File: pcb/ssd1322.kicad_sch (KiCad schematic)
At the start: 11 parts, among them J10 SSD1322 30-Pin Connector, J8 Display Connector Input, J9 Display Connector Output

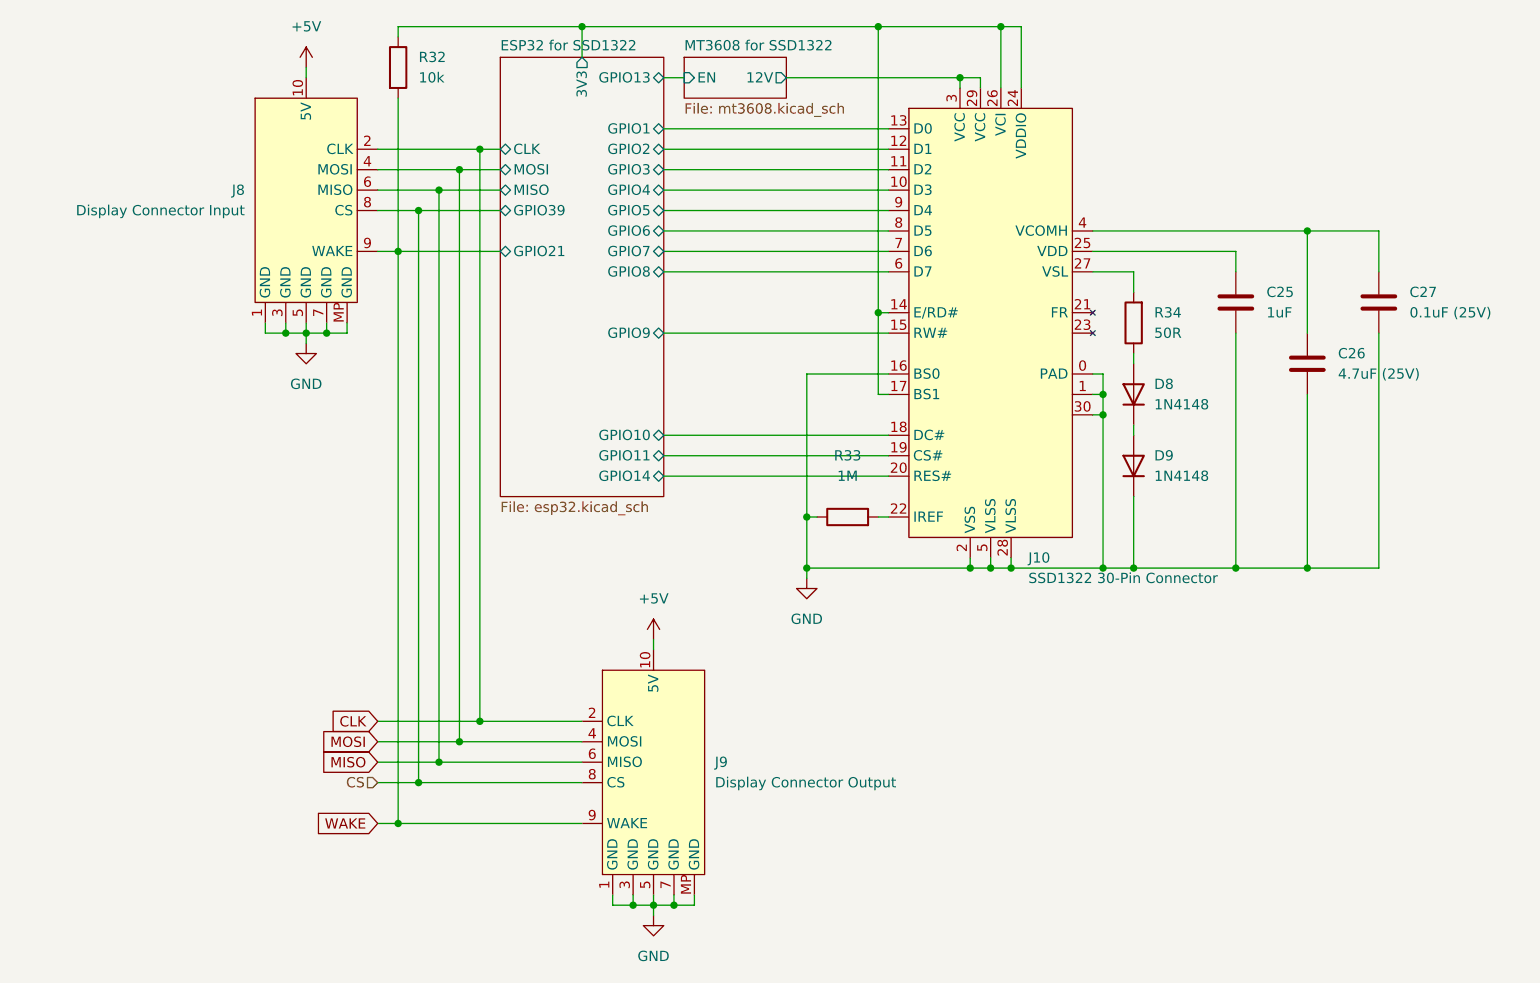
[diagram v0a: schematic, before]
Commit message: Split PCB into modules
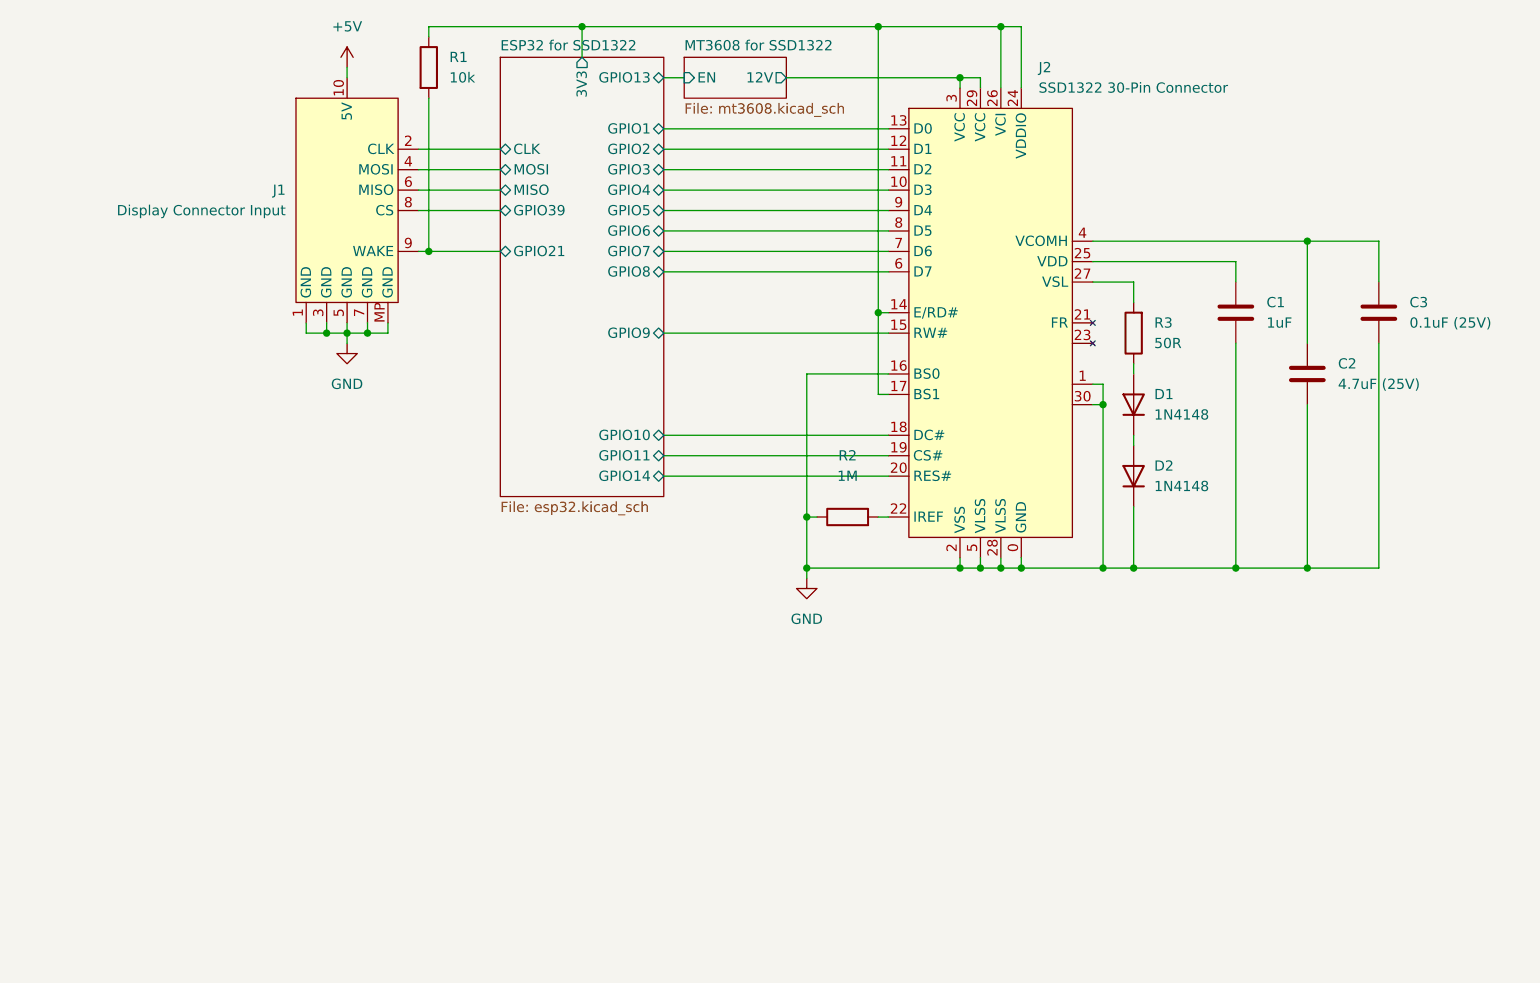
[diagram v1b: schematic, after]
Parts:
- removed J9: Display Connector Output, Connector_Molex:Molex_PicoBlade_53261-1071_1x10-1MP_P1.25mm_Horizontal, symbol Data Connector:Display_Connector_Output
- J2: renamed from J10; footprint Connector_FFC-FPC:TE_3-1734839-0_1x30-1MP_P0.5mm_Horizontal -> Display_FPC:ssd1322
- renumbered C25 to C1, C26 to C2, C27 to C3, D8 to D1, D9 to D2, J8 to J1, R32 to R1, R33 to R2, R34 to R3
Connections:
- net CLK renamed ESP32 for SSD1322/CLK
- net CS renamed ESP32 for SSD1322/GPIO39
- net MISO renamed ESP32 for SSD1322/MISO
- net MOSI renamed ESP32 for SSD1322/MOSI
- net WAKE renamed ESP32 for SSD1322/GPIO21
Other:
- moved on the sheet: C1, C2, C3, D1, D2, J1, R1, R3

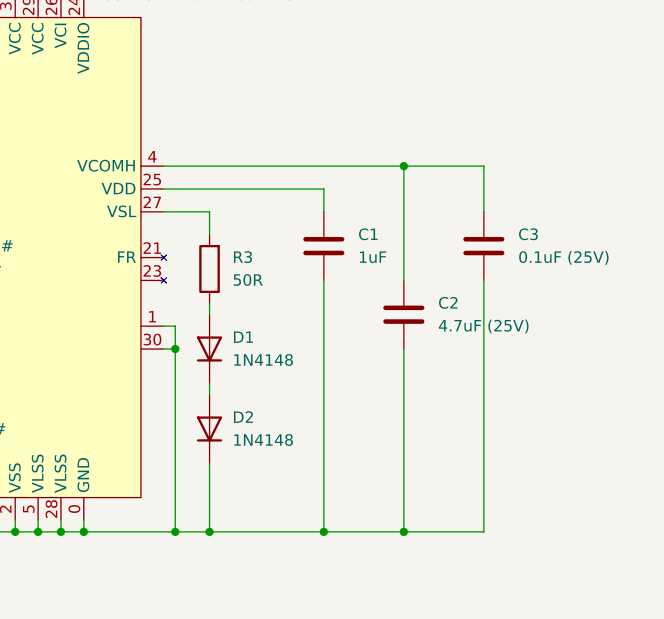
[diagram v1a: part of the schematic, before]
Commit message: Master board PCB routing
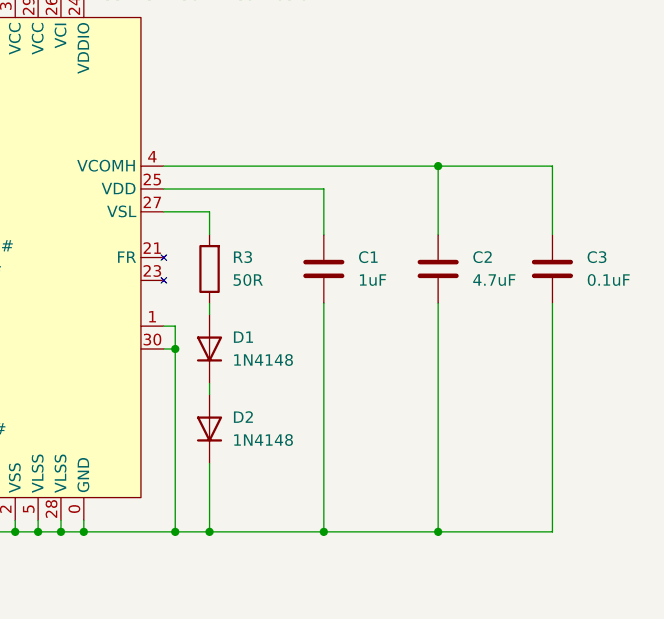
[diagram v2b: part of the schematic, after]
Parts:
- C2: value 4.7uF (25V) -> 4.7uF
- C3: value 0.1uF (25V) -> 0.1uF
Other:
- moved on the sheet: C1, C2, C3
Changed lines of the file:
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@@
+	)
+	(junction
+		(at 180.34 60.96)
+		(diameter 0)
+		(color 0 0 0 0)
+	)
+	(junction
+		(at 180.34 101.6)
+		(diameter 0)
+		(color 0 0 0 0)
 	)
 	(junction
@@
 	)
 	(junction
-		(at 176.53 101.6)
-		(diameter 0)
-		(color 0 0 0 0)
-	)
-	(junction
 		(at 123.19 69.85)
 		(diameter 0)
@@
 	)
 	(junction
-		(at 176.53 60.96)
-		(diameter 0)
-		(color 0 0 0 0)
-	)
-	(junction
 		(at 133.35 101.6)
 		(diameter 0)
@@
 	(wire
 		(pts
+			(xy 180.34 60.96) (xy 193.04 60.96)
+		)
+		(stroke
+			(width 0)
+			(type default)
+		)
+	)
+	(wire
+		(pts
 			(xy 149.86 66.04) (xy 154.94 66.04)
 		)
@@
 	(wire
 		(pts
-			(xy 176.53 60.96) (xy 176.53 73.66)
+			(xy 180.34 60.96) (xy 180.34 68.58)
 		)
 		(stroke
@@
 	(wire
 		(pts
-			(xy 176.53 81.28) (xy 176.53 101.6)
+			(xy 180.34 76.2) (xy 180.34 101.6)
 		)
 		(stroke
@@
 	(wire
 		(pts
-			(xy 176.53 60.96) (xy 185.42 60.96)
-		)
-		(stroke
-			(width 0)
-			(type default)
-		)
-	)
-	(wire
-		(pts
 			(xy 123.19 95.25) (xy 124.46 95.25)
 		)
@@
 	(wire
 		(pts
+			(xy 180.34 101.6) (xy 193.04 101.6)
+		)
+		(stroke
+			(width 0)
+			(type default)
+		)
+	)
+	(wire
+		(pts
 			(xy 135.89 101.6) (xy 138.43 101.6)
 		)
@@
 	(wire
 		(pts
-			(xy 167.64 63.5) (xy 167.64 66.04)
+			(xy 167.64 63.5) (xy 167.64 68.58)
 		)
 		(stroke
@@
 	(wire
 		(pts
-			(xy 167.64 101.6) (xy 176.53 101.6)
+			(xy 167.64 101.6) (xy 180.34 101.6)
 		)
 		(stroke
@@
 	(wire
 		(pts
-			(xy 176.53 101.6) (xy 185.42 101.6)
-		)
-		(stroke
-			(width 0)
-			(type default)
-		)
-	)
-	(wire
-		(pts
 			(xy 66.04 49.53) (xy 76.2 49.53)
 		)
@@
 	(wire
 		(pts
-			(xy 167.64 73.66) (xy 167.64 101.6)
+			(xy 167.64 76.2) (xy 167.64 101.6)
 		)
 		(stroke
@@
 	(wire
 		(pts
-			(xy 149.86 60.96) (xy 176.53 60.96)
+			(xy 149.86 60.96) (xy 180.34 60.96)
 		)
 		(stroke
@@
 	(wire
 		(pts
-			(xy 185.42 73.66) (xy 185.42 101.6)
+			(xy 193.04 76.2) (xy 193.04 101.6)
 		)
 		(stroke
@@
 	(wire
 		(pts
-			(xy 185.42 60.96) (xy 185.42 66.04)
+			(xy 193.04 60.96) (xy 193.04 68.58)
 		)
 		(stroke
@@
 	(symbol
 		(lib_id "Device:C")
-		(at 167.64 69.85 0)
+		(at 167.64 72.39 0)
 		(unit 1)
 		(exclude_from_sim no)
@@
 		(fields_autoplaced yes)
 		(property "Reference" "C1"
-			(at 171.45 68.5799 0)
+			(at 171.45 71.1199 0)
 			(effects
 				(font
@@
 		)
 		(property "Value" "1uF"
-			(at 171.45 71.1199 0)
+			(at 171.45 73.6599 0)
 			(effects
 				(font
@@
 		)
 		(property "Footprint" "Capacitor_SMD:C_0603_1608Metric"
-			(at 168.6052 73.66 0)
+			(at 168.6052 76.2 0)
 			(effects
 				(font
@@
 		)
 		(property "Datasheet" "~"
-			(at 167.64 69.85 0)
+			(at 167.64 72.39 0)
 			(effects
 				(font
@@
 		)
 		(property "Description" "Unpolarized capacitor"
-			(at 167.64 69.85 0)
+			(at 167.64 72.39 0)
 			(effects
 				(font
@@
 	(symbol
 		(lib_id "Device:C")
-		(at 185.42 69.85 0)
+		(at 193.04 72.39 0)
 		(unit 1)
 		(exclude_from_sim no)
@@
 		(fields_autoplaced yes)
 		(property "Reference" "C3"
-			(at 189.23 68.5799 0)
+			(at 196.85 71.1199 0)
 			(effects
 				(font
@@
 			)
 		)
-		(property "Value" "0.1uF (25V)"
-			(at 189.23 71.1199 0)
+		(property "Value" "0.1uF"
+			(at 196.85 73.6599 0)
 			(effects
 				(font
@@
 		)
 		(property "Footprint" "Capacitor_SMD:C_0603_1608Metric"
-			(at 186.3852 73.66 0)
+			(at 194.0052 76.2 0)
 			(effects
 				(font
@@
 		)
 		(property "Datasheet" "~"
-			(at 185.42 69.85 0)
+			(at 193.04 72.39 0)
 			(effects
 				(font
@@
 		)
 		(property "Description" "Unpolarized capacitor"
-			(at 185.42 69.85 0)
+			(at 193.04 72.39 0)
 			(effects
 				(font
@@
 	(symbol
 		(lib_id "Device:C")
-		(at 176.53 77.47 0)
+		(at 180.34 72.39 0)
 		(unit 1)
 		(exclude_from_sim no)
@@
 		(fields_autoplaced yes)
 		(property "Reference" "C2"
-			(at 180.34 76.1999 0)
+			(at 184.15 71.1199 0)
 			(effects
 				(font
@@
 			)
 		)
-		(property "Value" "4.7uF (25V)"
-			(at 180.34 78.7399 0)
+		(property "Value" "4.7uF"
+			(at 184.15 73.6599 0)
 			(effects
 				(font
@@
 		)
 		(property "Footprint" "Capacitor_SMD:C_0603_1608Metric"
-			(at 177.4952 81.28 0)
+			(at 181.3052 76.2 0)
 			(effects
 				(font
@@
 		)
 		(property "Datasheet" "~"
-			(at 176.53 77.47 0)
+			(at 180.34 72.39 0)
 			(effects
 				(font
@@
 		)
 		(property "Description" "Unpolarized capacitor"
-			(at 176.53 77.47 0)
-			(effects
-				(font
+			(at 180.34 72.39 0)
+			(effects
+				(font
